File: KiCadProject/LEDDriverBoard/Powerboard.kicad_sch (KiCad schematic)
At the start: 30 parts, among them J1 XT30, J2 XT30, J3 JST_SM04B, J4 JST_SM04B, Q1 Q_NMOS_GDS, Q2 SUD50P10-43L-GE3, U1 MAX16833

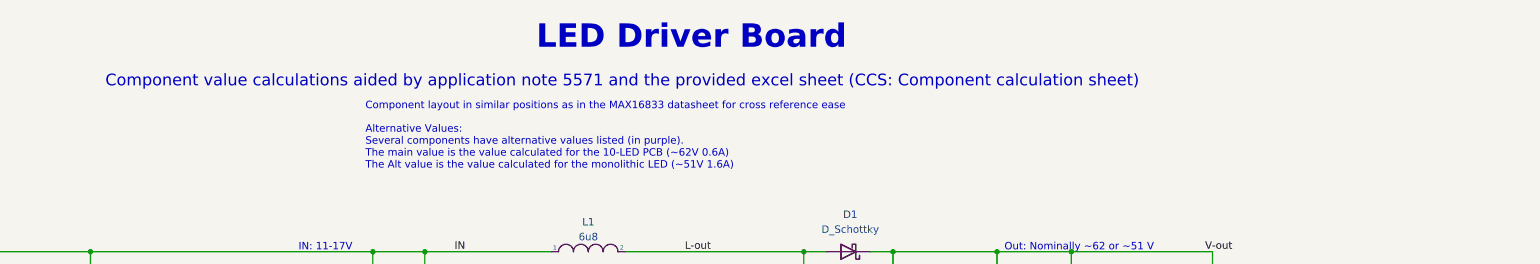
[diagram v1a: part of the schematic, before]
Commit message: Made ready to order PCBs. Some problems with ordering due to misunderstanding. Thinking about solutions
Signed-off-by: Eldalote.Electronics <Eldalote.Electronics@gmail.com>
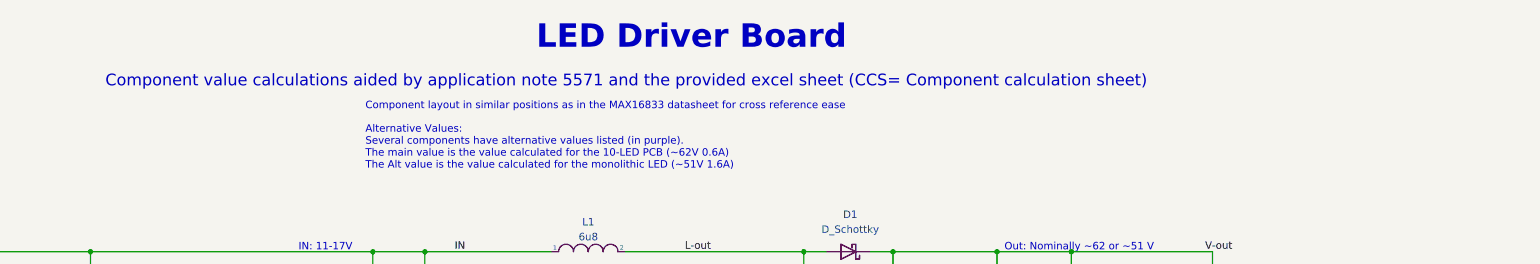
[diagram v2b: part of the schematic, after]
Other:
- note added: "Component value calculations aided by application note 5571 and the provided excel sheet (CCS= Component calculation sheet)"
- note removed: "Component value calculations aided by application note 5571 and the provided excel sheet (CCS: Component calculation sheet)"
- company: (none) -> Eldalote Electronics
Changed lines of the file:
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@@
     (date "2023-02-01")
     (rev "V0.3")
+    (company "Eldalote Electronics")
     (comment 1 "many of the functions of the dive lamp have been split onto different PCBs")
     (comment 2 "Due to tight radius constrains, ")
-    (comment 4 "Part of the Dive lamp overall design")
+    (comment 4 "Part of the Dive lamp design")
   )
   (junction (at 198.12 90.17) (diameter 0) (color 0 0 0 0)
@@
     (effects (font (size 4 4) (thickness 0.8) bold) (justify left bottom))
   )
-  (text "Component value calculations aided by application note 5571 and the provided excel sheet (CCS: Component calculation sheet)\n"
+  (text "Component value calculations aided by application note 5571 and the provided excel sheet (CCS= Component calculation sheet)\n"
     (at 45.72 34.29 0)
     (effects (font (size 2 2)) (justify left bottom))
